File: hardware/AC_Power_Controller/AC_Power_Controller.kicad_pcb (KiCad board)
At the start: 2 copper layers, 20 parts, among them J1 230VAC_IN, U1 MOC3023M, U2 ADS1115IDGS, U3 ZMPT101B, U4 PC814, U5 SCT_013_030

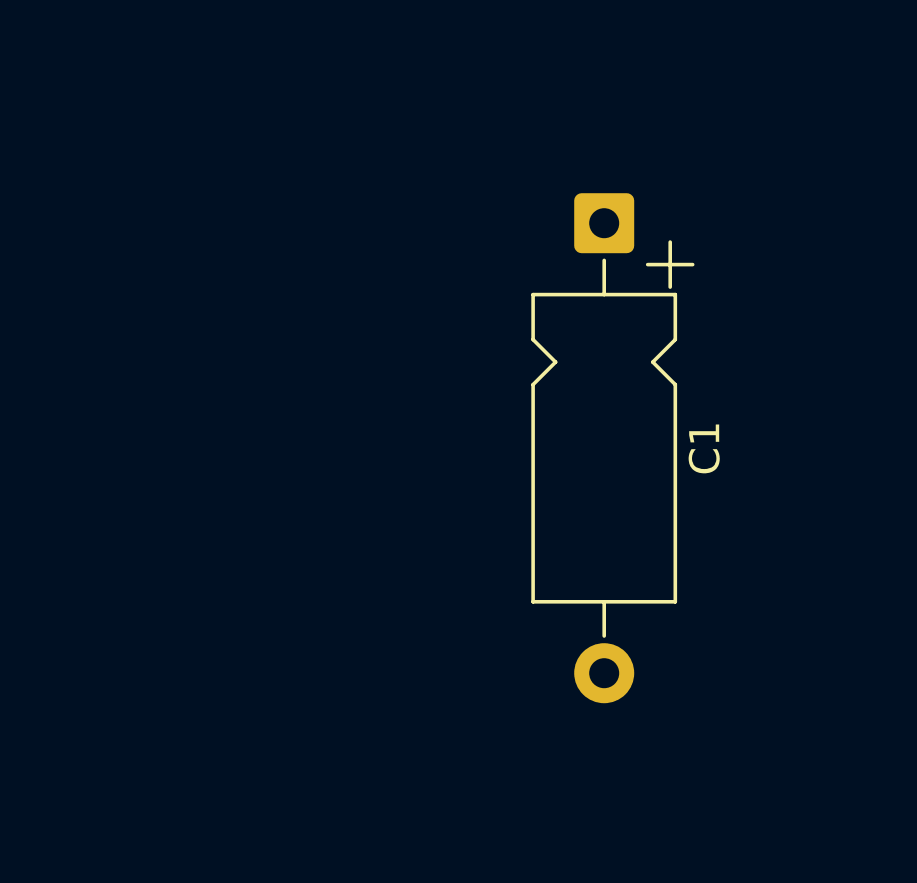
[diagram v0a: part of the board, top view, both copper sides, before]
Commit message: corrections to schematics
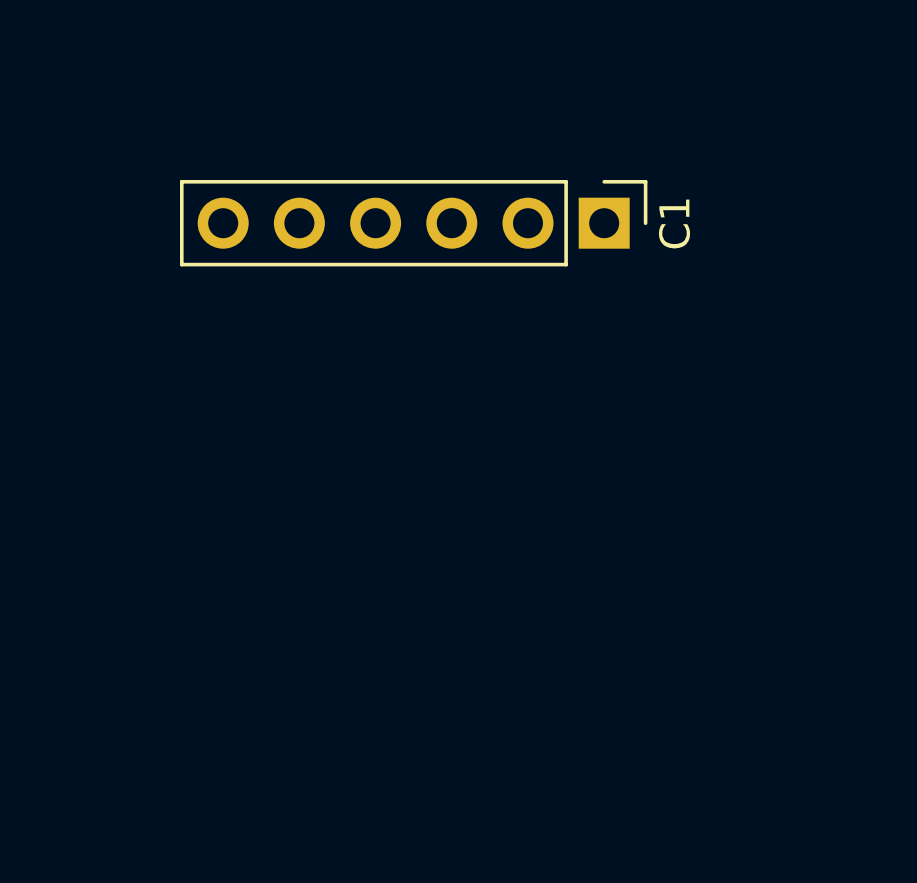
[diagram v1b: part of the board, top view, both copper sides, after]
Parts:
- C1: footprint Capacitor_THT:CP_Axial_L10.0mm_D4.5mm_P15.00mm_Horizontal -> Connector_PinHeader_2.54mm:PinHeader_1x06_P2.54mm_Vertical
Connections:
- A1 pad 9: unconnected-(A1-A0-Pad9) -> Net-(A1-A0)
- R7 pad 1: Net-(U3-OUT) -> Net-(A1-A0)
- U3 pad 4: Net-(U3-OUT) -> Net-(A1-A0)
